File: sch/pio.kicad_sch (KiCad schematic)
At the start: 18 parts, among them X2 I/O connector

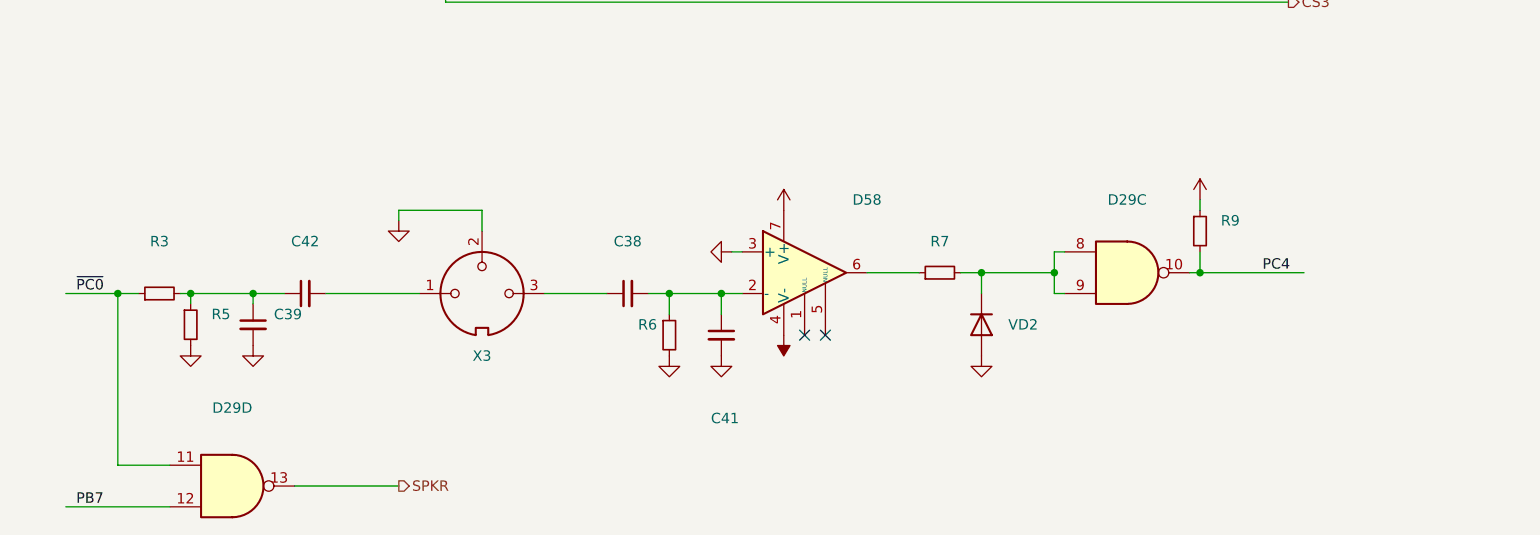
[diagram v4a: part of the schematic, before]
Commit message: Schematics completed with values
Visual corrections pending
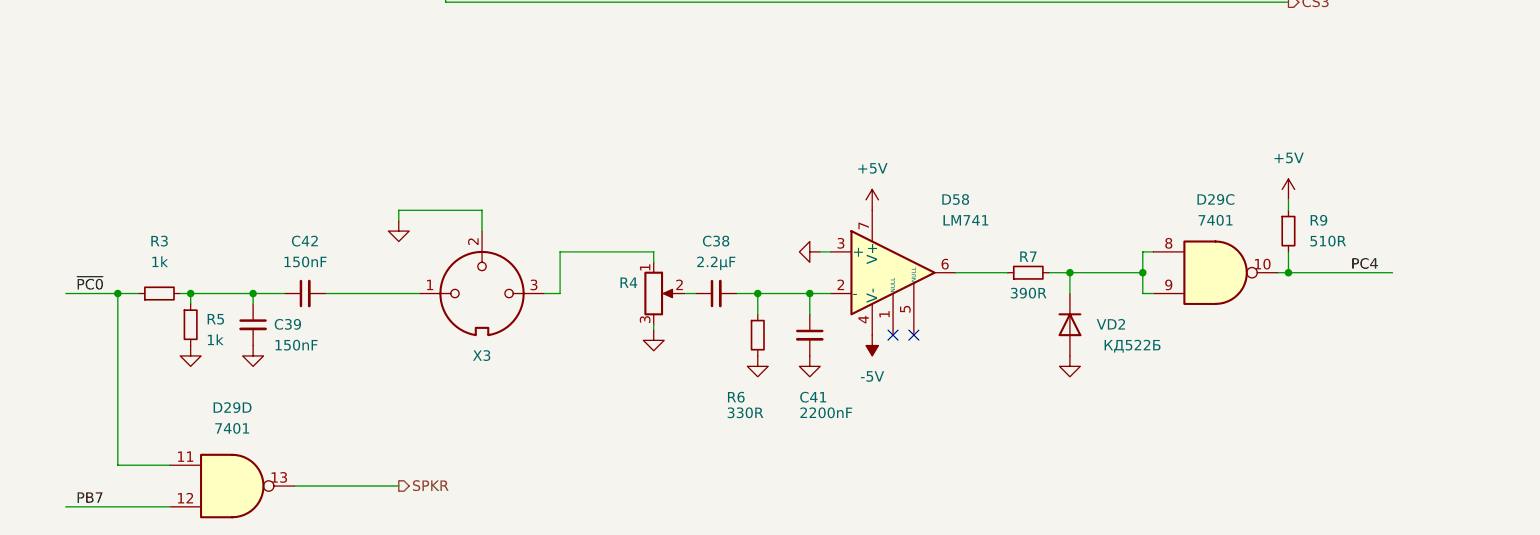
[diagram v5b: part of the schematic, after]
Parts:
- added R4: (no value), symbol Device:R_Potentiometer
- C38: value ~ -> 2.2μF
- C39, C42: value ~ -> 150nF
- C41: value ~ -> 2200nF
- D29: value (none) -> 7401; CCCP (none) -> К155ЛА8
- D58: value ~ -> LM741; CCCP (none) -> УД708
- R3, R5: value ~ -> 1k
- R6: value ~ -> 330R
- R7: value ~ -> 390R
- R9: value ~ -> 510R
- VD2: value ~ -> КД522Б
- X3: value ~ -> (none)
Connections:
- net GND: now also R4.3
- net at X3.3: now also R4.1; no longer C38.1
- new net: C38.1, R4.2
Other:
- moved on the sheet: C38, C41, D29C, D58, R6, R7, R9, VD2

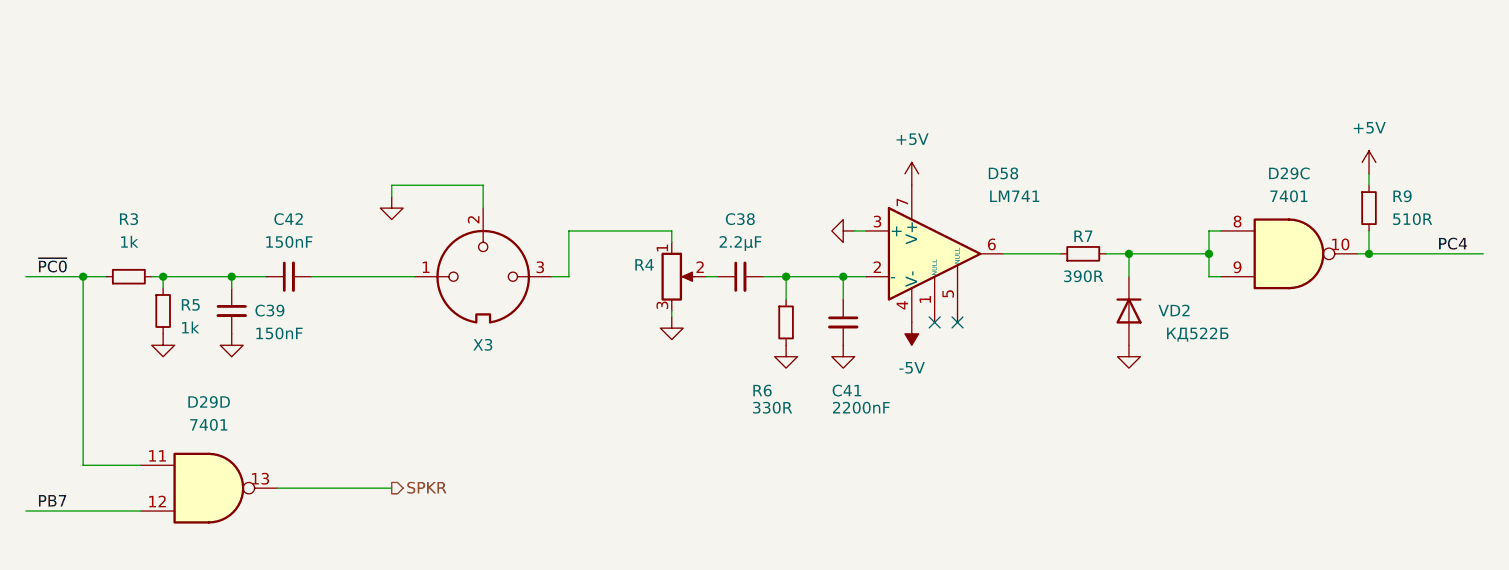
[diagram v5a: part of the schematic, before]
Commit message: Sch: visual corrections
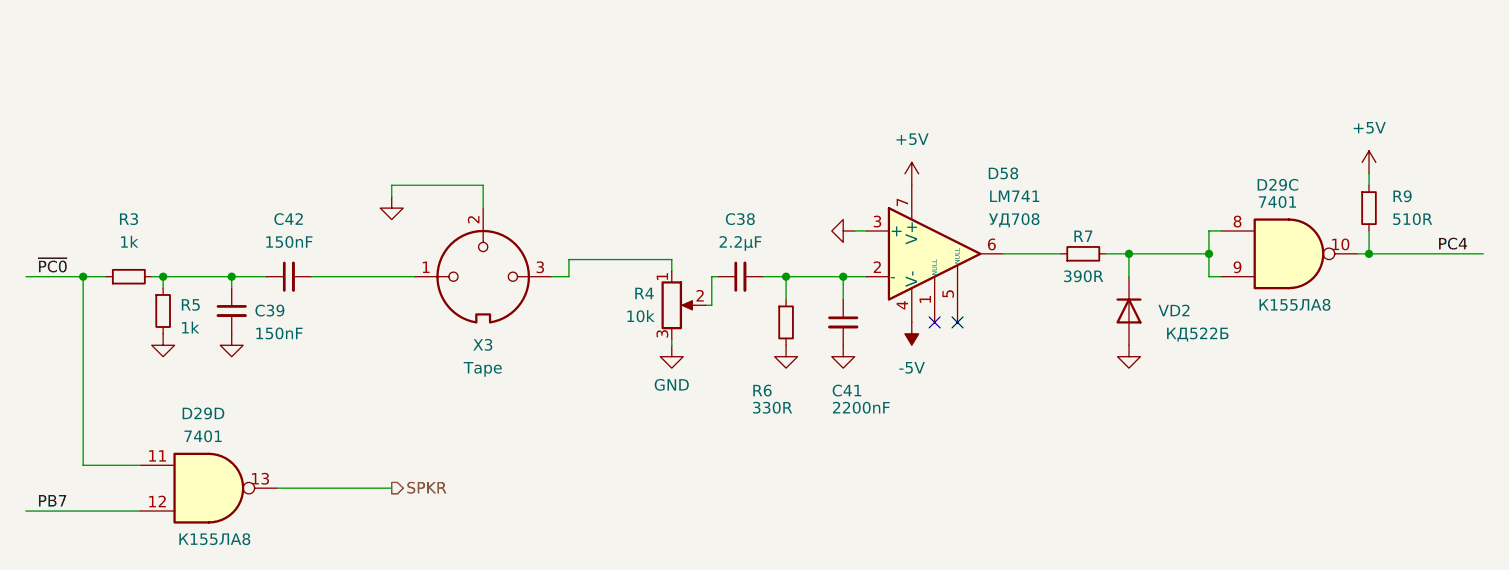
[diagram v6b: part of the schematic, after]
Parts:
- R4: value (none) -> 10k
- X3: value (none) -> Tape
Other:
- moved on the sheet: R4
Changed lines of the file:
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@@
     (stroke (width 0) (type default) (color 0 0 0 0))
   )
-  (wire (pts (xy 108.585 154.94) (xy 108.585 155.575))
+  (wire (pts (xy 108.585 158.115) (xy 108.585 158.75))
     (stroke (width 0) (type default) (color 0 0 0 0))
   )
@@
     (stroke (width 0) (type default) (color 0 0 0 0))
   )
-  (wire (pts (xy 112.395 151.13) (xy 113.665 151.13))
-    (stroke (width 0) (type default) (color 0 0 0 0))
-  )
   (wire (pts (xy 133.985 77.47) (xy 151.765 77.47))
     (stroke (width 0) (type default) (color 0 0 0 0))
@@
     (stroke (width 0) (type default) (color 0 0 0 0))
   )
+  (wire (pts (xy 113.03 154.305) (xy 112.395 154.305))
+    (stroke (width 0) (type default) (color 0 0 0 0))
+  )
   (wire (pts (xy 85.725 81.28) (xy 85.725 113.03))
     (stroke (width 0) (type default) (color 0 0 0 0))
@@
     (stroke (width 0) (type default) (color 0 0 0 0))
   )
+  (wire (pts (xy 113.03 154.305) (xy 113.03 151.13))
+    (stroke (width 0) (type default) (color 0 0 0 0))
+  )
   (wire (pts (xy 114.935 90.17) (xy 113.665 90.17))
     (stroke (width 0) (type default) (color 0 0 0 0))
@@
     (stroke (width 0) (type default) (color 0 0 0 0))
   )
-  (wire (pts (xy 108.585 146.05) (xy 108.585 147.32))
+  (wire (pts (xy 108.585 149.225) (xy 108.585 150.495))
     (stroke (width 0) (type default) (color 0 0 0 0))
   )
@@
     (stroke (width 0) (type default) (color 0 0 0 0))
   )
+  (wire (pts (xy 113.03 151.13) (xy 113.665 151.13))
+    (stroke (width 0) (type default) (color 0 0 0 0))
+  )
   (wire (pts (xy 168.275 151.13) (xy 169.545 151.13))
     (stroke (width 0) (type default) (color 0 0 0 0))
@@
     (stroke (width 0) (type default) (color 0 0 0 0))
   )
-  (wire (pts (xy 97.155 146.05) (xy 108.585 146.05))
+  (wire (pts (xy 97.155 149.225) (xy 108.585 149.225))
     (stroke (width 0) (type default) (color 0 0 0 0))
   )
@@
     (stroke (width 0) (type default) (color 0 0 0 0))
   )
-  (wire (pts (xy 97.155 151.13) (xy 97.155 146.05))
+  (wire (pts (xy 97.155 151.13) (xy 97.155 149.225))
     (stroke (width 0) (type default) (color 0 0 0 0))
   )
@@
     (in_bom yes) (on_board yes) (fields_autoplaced)
     (property "Reference" "X3" (id 0) (at 87.6301 158.75 0))
-    (property "Value" "" (id 1) (at 87.6301 161.29 0))
+    (property "Value" "Tape" (id 1) (at 87.6301 161.29 0))
     (property "Footprint" "" (id 2) (at 87.63 151.13 0)
       (effects (font (size 1.27 1.27)) hide)
@@
   )
   (symbol (lib_id "74xx:74LS01") (at 177.165 148.59 0) (unit 3)
-    (in_bom yes) (on_board yes) (fields_autoplaced)
-    (property "Reference" "D29" (id 0) (at 177.165 139.7 0))
-    (property "Value" "7401" (id 1) (at 177.165 142.24 0))
+    (in_bom yes) (on_board yes)
+    (property "Reference" "D29" (id 0) (at 175.895 140.97 0))
+    (property "Value" "7401" (id 1) (at 175.895 142.875 0))
     (property "Footprint" "" (id 2) (at 177.165 148.59 0)
       (effects (font (size 1.27 1.27)) hide)
@@
       (effects (font (size 1.27 1.27)) hide)
     )
-    (property "CCCP" "К155ЛА8" (id 4) (at 177.165 148.59 0)
-      (effects (font (size 1.27 1.27)) hide)
-    )
+    (property "CCCP" "К155ЛА8" (id 4) (at 177.8 154.305 0))
     (pin "1")
     (pin "2")
@@
       (effects (font (size 1.27 1.27)) hide)
     )
-    (property "CCCP" "УД708" (id 4) (at 137.795 148.59 0)
-      (effects (font (size 1.27 1.27)) hide)
-    )
+    (property "CCCP" "УД708" (id 4) (at 146.685 144.78 0))
     (pin "1")
     (pin "2")
@@
   )
   (symbol (lib_id "74xx:74LS01") (at 57.15 174.625 0) (unit 4)
-    (in_bom yes) (on_board yes) (fields_autoplaced)
-    (property "Reference" "D29" (id 0) (at 57.15 165.1 0))
-    (property "Value" "7401" (id 1) (at 57.15 167.64 0))
+    (in_bom yes) (on_board yes)
+    (property "Reference" "D29" (id 0) (at 56.515 166.37 0))
+    (property "Value" "7401" (id 1) (at 56.515 168.91 0))
     (property "Footprint" "" (id 2) (at 57.15 174.625 0)
       (effects (font (size 1.27 1.27)) hide)
@@
       (effects (font (size 1.27 1.27)) hide)
     )
-    (property "CCCP" "К155ЛА8" (id 4) (at 57.15 174.625 0)
-      (effects (font (size 1.27 1.27)) hide)
-    )
+    (property "CCCP" "К155ЛА8" (id 4) (at 57.785 180.34 0))
     (pin "1")
     (pin "2")
@@
     (pin "9")
   )
-  (symbol (lib_id "power:GND") (at 108.585 155.575 0) (unit 1)
+  (symbol (lib_id "power:GND") (at 108.585 158.75 0) (unit 1)
     (in_bom yes) (on_board yes) (fields_autoplaced)
-    (property "Reference" "#PWR?" (id 0) (at 108.585 161.925 0)
-      (effects (font (size 1.27 1.27)) hide)
-    )
-    (property "Value" "" (id 1) (at 108.585 160.02 0))
-    (property "Footprint" "" (id 2) (at 108.585 155.575 0)
-      (effects (font (size 1.27 1.27)) hide)
-    )
-    (property "Datasheet" "" (id 3) (at 108.585 155.575 0)
+    (property "Reference" "#PWR?" (id 0) (at 108.585 165.1 0)
+      (effects (font (size 1.27 1.27)) hide)
+    )
+    (property "Value" "GND" (id 1) (at 108.585 163.195 0))
+    (property "Footprint" "" (id 2) (at 108.585 158.75 0)
+      (effects (font (size 1.27 1.27)) hide)
+    )
+    (property "Datasheet" "" (id 3) (at 108.585 158.75 0)
       (effects (font (size 1.27 1.27)) hide)
     )
@@
     (pin "9")
   )
-  (symbol (lib_id "Device:R_Potentiometer") (at 108.585 151.13 0) (unit 1)
+  (symbol (lib_id "Device:R_Potentiometer") (at 108.585 154.305 0) (unit 1)
     (in_bom yes) (on_board yes) (fields_autoplaced)
-    (property "Reference" "R4" (id 0) (at 106.68 149.8599 0)
+    (property "Reference" "R4" (id 0) (at 106.68 153.0349 0)
       (effects (font (size 1.27 1.27)) (justify right))
     )
-    (property "Value" "" (id 1) (at 106.68 152.3999 0)
+    (property "Value" "10k" (id 1) (at 106.68 155.5749 0)
       (effects (font (size 1.27 1.27)) (justify right))
     )
-    (property "Footprint" "" (id 2) (at 108.585 151.13 0)
-      (effects (font (size 1.27 1.27)) hide)
-    )
-    (property "Datasheet" "~" (id 3) (at 108.585 151.13 0)
-      (effects (font (size 1.27 1.27)) hide)
-    )
+    (property "Footprint" "" (id 2) (at 108.585 154.305 0)
+      (effects (font (size 1.27 1.27)) hide)
+    )
+    (property "Datasheet" "~" (id 3) (at 108.585 154.305 0)
+      (effects (font (size 1.27 1.27)) hide)
+    )
